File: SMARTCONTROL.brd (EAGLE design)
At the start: 40 x 50 mm, 37 parts, among them IC1 ESP12SMT, Q2 RJU003N03, Q3 RJU003N03, Q4 RJU003N03, Q5 RJU003N03

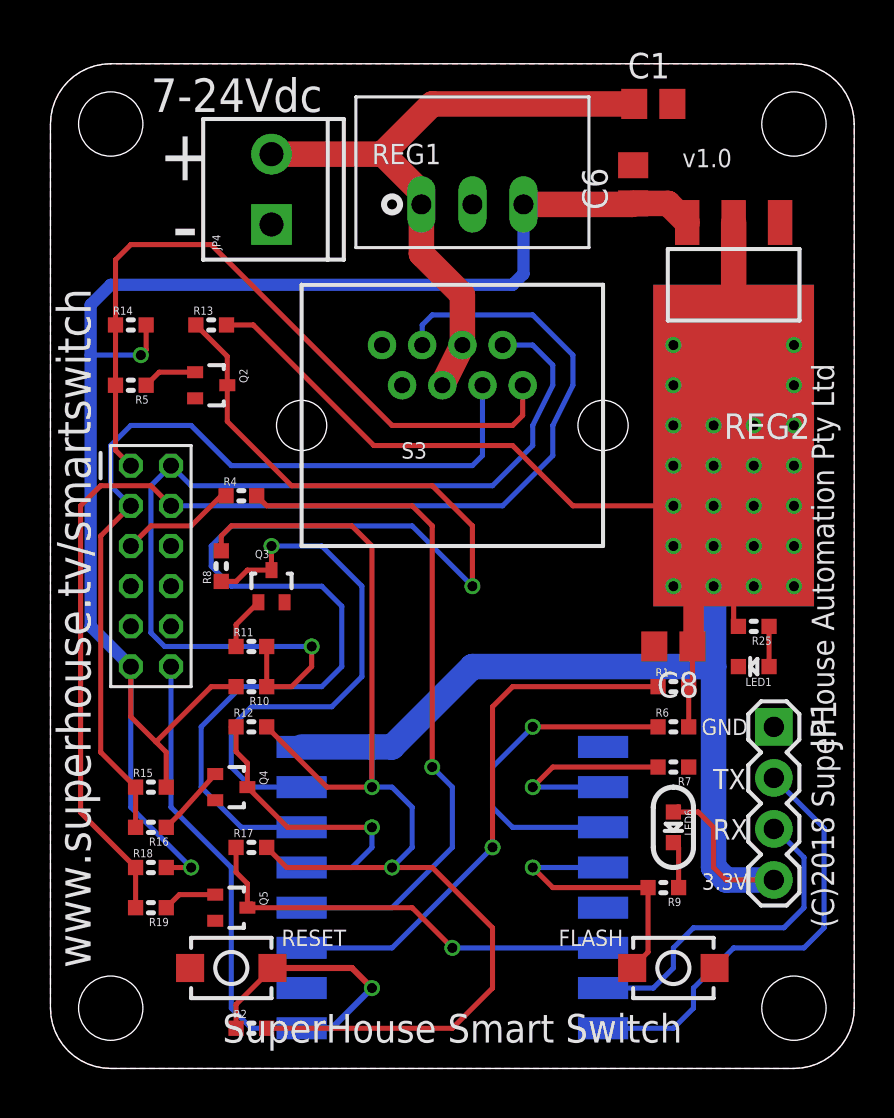
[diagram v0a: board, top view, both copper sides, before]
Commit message: Fixed ESP-12 footprint (swapped D4/5)
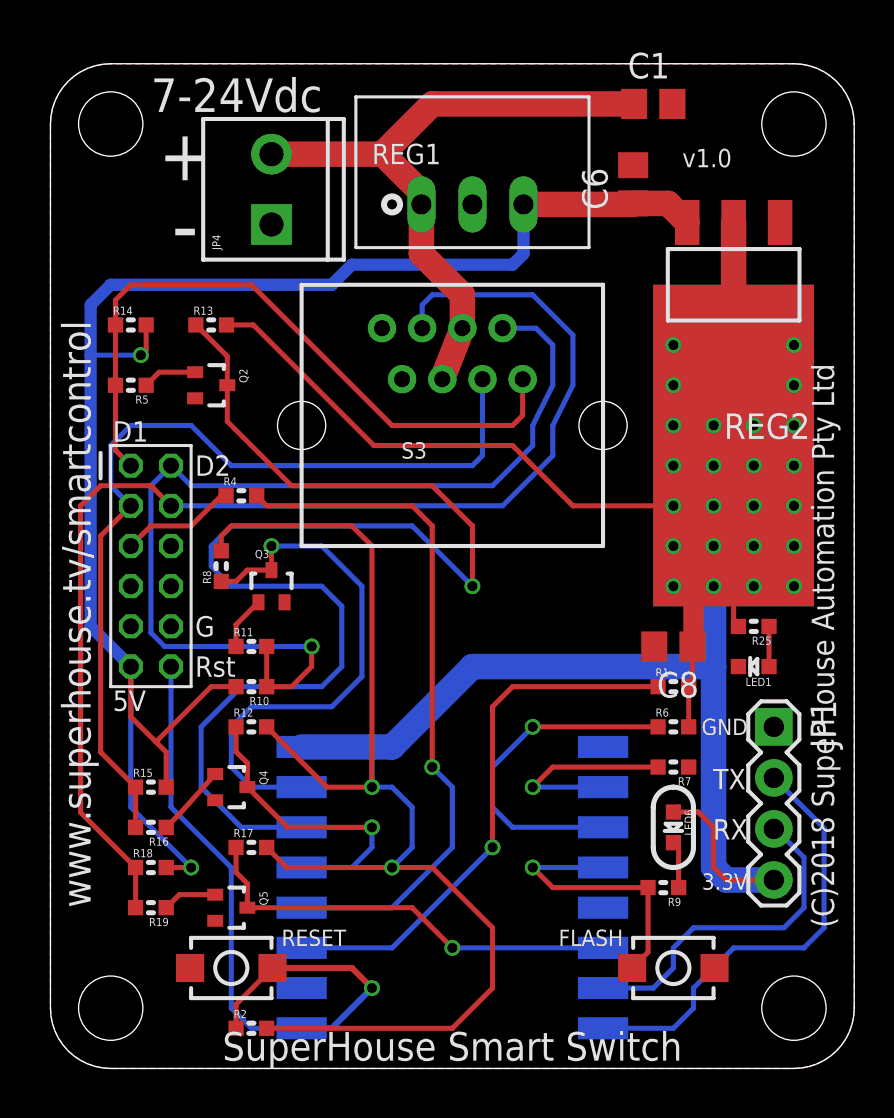
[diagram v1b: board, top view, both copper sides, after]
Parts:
- R4: value 330R -> 100R
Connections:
- net GPIO4: now also IC1.13; no longer IC1.14, Q5.3, R17.1
- net GPIO5: now also IC1.14, Q5.3, R17.1; no longer IC1.13
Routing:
- net GPIO4: track 22.0 -> 0.00 mm, vias 1 -> 0
- net GPIO5: track 0.00 -> 21.8 mm, vias 0 -> 1
- net BUTTON1: track 36.6 -> 34.0 mm
- net BUTTON4: track 61.3 -> 62.4 mm
- net BUTTON2: track 49.1 -> 50.0 mm
- net 5V: track 81.5 -> 80.9 mm
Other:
- board text added: "5V"
- board text added: "D1"
- board text added: "D2"
- board text added: "G"
- board text added: "Rst"
- board text added: "www.superhouse.tv/smartcontrol"
- board text removed: "www.superhouse.tv/smartswitch"
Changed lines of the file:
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@@
 <text x="39" y="7" size="1.1176" layer="21" font="vector" ratio="15" rot="R90">(C)2018 SuperHouse Automation Pty Ltd</text>
 <text x="31.4452" y="44.8486" size="0.9144" layer="21" font="vector" ratio="15">v1.0</text>
-<text x="20" y="2" size="1.4224" layer="21" font="vector" ratio="15" align="center">SuperHouse Smart Switch</text>
-<text x="2" y="5" size="1.6764" layer="21" font="vector" ratio="15" rot="R90">www.superhouse.tv/smartswitch</text>
+<text x="20" y="1.1" size="1.4224" layer="21" font="vector" ratio="15" align="center">SuperHouse Smart Switch</text>
+<text x="2" y="8" size="1.4224" layer="21" font="vector" ratio="15" rot="R90">www.superhouse.tv/smartcontrol</text>
 <hole x="3" y="3" drill="3.2"/>
 <hole x="3" y="47" drill="3.2"/>
@@
 <text x="11.5" y="6.5" size="0.8128" layer="21" font="vector" ratio="14" align="center-left">RESET</text>
 <text x="28.5" y="6.5" size="0.8128" layer="21" font="vector" ratio="14" align="center-right">FLASH</text>
+<text x="7.2" y="30" size="1.016" layer="21" font="vector" ratio="18" align="center-left">D2</text>
+<text x="7.2" y="22" size="1.016" layer="21" font="vector" ratio="18" align="center-left">G</text>
+<text x="7.2" y="20" size="1.016" layer="21" font="vector" ratio="18" align="center-left">Rst</text>
+<text x="3.1" y="31.7" size="1.016" layer="21" font="vector" ratio="18" align="center-left">D1</text>
+<text x="3.1" y="18.3" size="1.016" layer="21" font="vector" ratio="18" align="center-left">5V</text>
 </plain>
 <attributes>
@@
 </autorouter>
 <elements>
-<element name="R4" library="freetronics-master-v1" package="0603" value="330R" x="9.5" y="28.5"/>
+<element name="R4" library="freetronics-master-v1" package="0603" value="100R" x="9.5" y="28.5"/>
 <element name="IC1" library="freetronics-jon" package="ESP12" value="ESP12SMT" x="20" y="6" rot="MR90"/>
 <element name="R1" library="freetronics-jon" package="0603" value="10k" x="31" y="19"/>
@@
 <wire x1="5.25" y1="16.25" x2="4" y2="17.5" width="0.254" layer="1"/>
 <wire x1="4" y1="17.5" x2="4" y2="20" width="0.254" layer="1"/>
-<wire x1="3" y1="39" x2="23" y2="39" width="0.6096" layer="16"/>
-<wire x1="23" y1="39" x2="23.54" y2="39.54" width="0.6096" layer="16"/>
-<wire x1="23.54" y1="39.54" x2="23.54" y2="43" width="0.6096" layer="16"/>
+<wire x1="3" y1="39" x2="14" y2="39" width="0.6096" layer="16"/>
+<wire x1="14" y1="39" x2="15" y2="40" width="0.6096" layer="16"/>
+<wire x1="15" y1="40" x2="23" y2="40" width="0.6096" layer="16"/>
+<wire x1="23" y1="40" x2="23.54" y2="40.54" width="0.6096" layer="16"/>
+<wire x1="23.54" y1="40.54" x2="23.54" y2="43" width="0.6096" layer="16"/>
 <wire x1="5.762" y1="10" x2="7" y2="10" width="0.254" layer="1"/>
 <via x="7" y="10" extent="1-16" drill="0.5"/>
@@
 </signal>
 <signal name="GPIO5">
-<contactref element="IC1" pad="13"/>
-</signal>
-<signal name="GPIO4">
 <contactref element="IC1" pad="14"/>
 <contactref element="Q5" pad="3"/>
 <contactref element="R17" pad="1"/>
+<wire x1="9.238" y1="11" x2="9.238" y2="9.762" width="0.254" layer="1"/>
+<wire x1="9.8" y1="9.2" x2="9.8" y2="8" width="0.254" layer="1"/>
+<wire x1="9.238" y1="9.762" x2="9.8" y2="9.2" width="0.254" layer="1"/>
 <wire x1="9.8" y1="8" x2="18" y2="8" width="0.254" layer="1"/>
 <wire x1="18" y1="8" x2="20" y2="6" width="0.254" layer="1"/>
 <via x="20" y="6" extent="1-16" drill="0.5"/>
 <wire x1="20" y1="6" x2="27.5" y2="6" width="0.254" layer="16"/>
-<wire x1="9.8" y1="8" x2="10" y2="8.2" width="0.254" layer="1"/>
-<wire x1="9.238" y1="11" x2="9.238" y2="9.762" width="0.254" layer="1"/>
-<wire x1="9.8" y1="9.2" x2="9.8" y2="8" width="0.254" layer="1"/>
-<wire x1="9.238" y1="9.762" x2="9.8" y2="9.2" width="0.254" layer="1"/>
+</signal>
+<signal name="GPIO4">
+<contactref element="IC1" pad="13"/>
 </signal>
 <signal name="GPIO14">
@@
 <wire x1="6" y1="28" x2="22.5" y2="28" width="0.254" layer="16"/>
 <wire x1="22.5" y1="28" x2="25" y2="30.5" width="0.254" layer="16"/>
-<wire x1="26" y1="35.5" x2="24" y2="37.5" width="0.254" layer="16"/>
-<wire x1="24" y1="37.5" x2="19" y2="37.5" width="0.254" layer="16"/>
-<wire x1="19" y1="37.5" x2="18.5" y2="37" width="0.254" layer="16"/>
-<wire x1="18.5" y1="37" x2="18.5" y2="36" width="0.254" layer="16"/>
+<wire x1="26" y1="36.5" x2="24" y2="38.5" width="0.254" layer="16"/>
+<wire x1="24" y1="38.5" x2="19" y2="38.5" width="0.254" layer="16"/>
+<wire x1="19" y1="38.5" x2="18.5" y2="38" width="0.254" layer="16"/>
+<wire x1="18.5" y1="38" x2="18.5" y2="36.84" width="0.254" layer="16"/>
 <wire x1="25" y1="30.5" x2="25" y2="32" width="0.254" layer="16"/>
 <wire x1="25" y1="32" x2="26" y2="34" width="0.254" layer="16"/>
-<wire x1="26" y1="34" x2="26" y2="35.5" width="0.254" layer="16"/>
+<wire x1="26" y1="34" x2="26" y2="36.5" width="0.254" layer="16"/>
 </signal>
 <signal name="BUTTON1">
@@
 <contactref element="H1" pad="1"/>
 <wire x1="3.238" y1="37" x2="3.238" y2="34" width="0.254" layer="1"/>
-<wire x1="23.5" y1="34" x2="23.5" y2="32.5" width="0.254" layer="1"/>
+<wire x1="23.5" y1="34.3" x2="23.5" y2="32.5" width="0.254" layer="1"/>
 <wire x1="23.5" y1="32.5" x2="23" y2="32" width="0.254" layer="1"/>
 <wire x1="23" y1="32" x2="17" y2="32" width="0.254" layer="1"/>
-<wire x1="17" y1="32" x2="8" y2="41" width="0.254" layer="1"/>
-<wire x1="4" y1="41" x2="3.238" y2="40.238" width="0.254" layer="1"/>
-<wire x1="3.238" y1="40.238" x2="3.238" y2="37" width="0.254" layer="1"/>
-<wire x1="8" y1="41" x2="4" y2="41" width="0.254" layer="1"/>
+<wire x1="17" y1="32" x2="10" y2="39" width="0.254" layer="1"/>
+<wire x1="4" y1="39" x2="3.238" y2="38.238" width="0.254" layer="1"/>
+<wire x1="3.238" y1="38.238" x2="3.238" y2="37" width="0.254" layer="1"/>
+<wire x1="10" y1="39" x2="4" y2="39" width="0.254" layer="1"/>
 <wire x1="3.238" y1="34" x2="3.238" y2="30.762" width="0.254" layer="1"/>
 <wire x1="3.238" y1="30.762" x2="4" y2="30" width="0.254" layer="1"/>
@@
 <wire x1="24" y1="31" x2="24" y2="32" width="0.254" layer="16"/>
 <wire x1="24" y1="32" x2="25" y2="34" width="0.254" layer="16"/>
-<wire x1="25" y1="34" x2="25" y2="35" width="0.254" layer="16"/>
-<wire x1="25" y1="35" x2="24" y2="36" width="0.254" layer="16"/>
-<wire x1="24" y1="36" x2="22.5" y2="36" width="0.254" layer="16"/>
+<wire x1="25" y1="34" x2="25" y2="36" width="0.254" layer="16"/>
 <wire x1="5" y1="29" x2="6" y2="30" width="0.254" layer="16"/>
 <via x="13" y="21" extent="1-16" drill="0.5"/>
@@
 <wire x1="5.67996875" y1="21" x2="5" y2="21.67996875" width="0.254" layer="16"/>
 <wire x1="5" y1="21.67996875" x2="5" y2="29" width="0.254" layer="16"/>
+<wire x1="25" y1="36" x2="24.16" y2="36.84" width="0.254" layer="16"/>
+<wire x1="24.16" y1="36.84" x2="22.5" y2="36.84" width="0.254" layer="16"/>
 </signal>
 <signal name="BUTTON3">
@@
 <wire x1="9" y1="30" x2="21" y2="30" width="0.254" layer="16"/>
 <wire x1="21" y1="30" x2="21.5" y2="30.5" width="0.254" layer="16"/>
-<wire x1="21.5" y1="30.5" x2="21.5" y2="34" width="0.254" layer="16"/>
+<wire x1="21.5" y1="30.5" x2="21.5" y2="34.3" width="0.254" layer="16"/>
 <wire x1="7" y1="32" x2="9" y2="30" width="0.254" layer="16"/>
 <wire x1="4" y1="28" x2="3" y2="29" width="0.254" layer="16"/>
@@
 <wire x1="18.46" y1="43" x2="18.46" y2="43.59" width="1.27" layer="1"/>
 <wire x1="18.46" y1="43.59" x2="16.55" y2="45.5" width="1.27" layer="1"/>
-<wire x1="19.5" y1="34" x2="20.5" y2="36" width="1.27" layer="1"/>
+<wire x1="19.5" y1="34.3" x2="20.5" y2="36.84" width="1.27" layer="1"/>
 <wire x1="18.46" y1="40.54" x2="18.46" y2="43" width="1.27" layer="1"/>
-<wire x1="20.5" y1="36" x2="20.5" y2="38.5" width="1.27" layer="1"/>
+<wire x1="20.5" y1="36.84" x2="20.5" y2="38.5" width="1.27" layer="1"/>
 <wire x1="20.5" y1="38.5" x2="18.46" y2="40.54" width="1.27" layer="1"/>
 </signal>
@@
 </signal>
 </signals>
+<errors>
+</errors>
 </board>
 </drawing>

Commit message: Replaced most parts using SuperHouse library to add 3D models
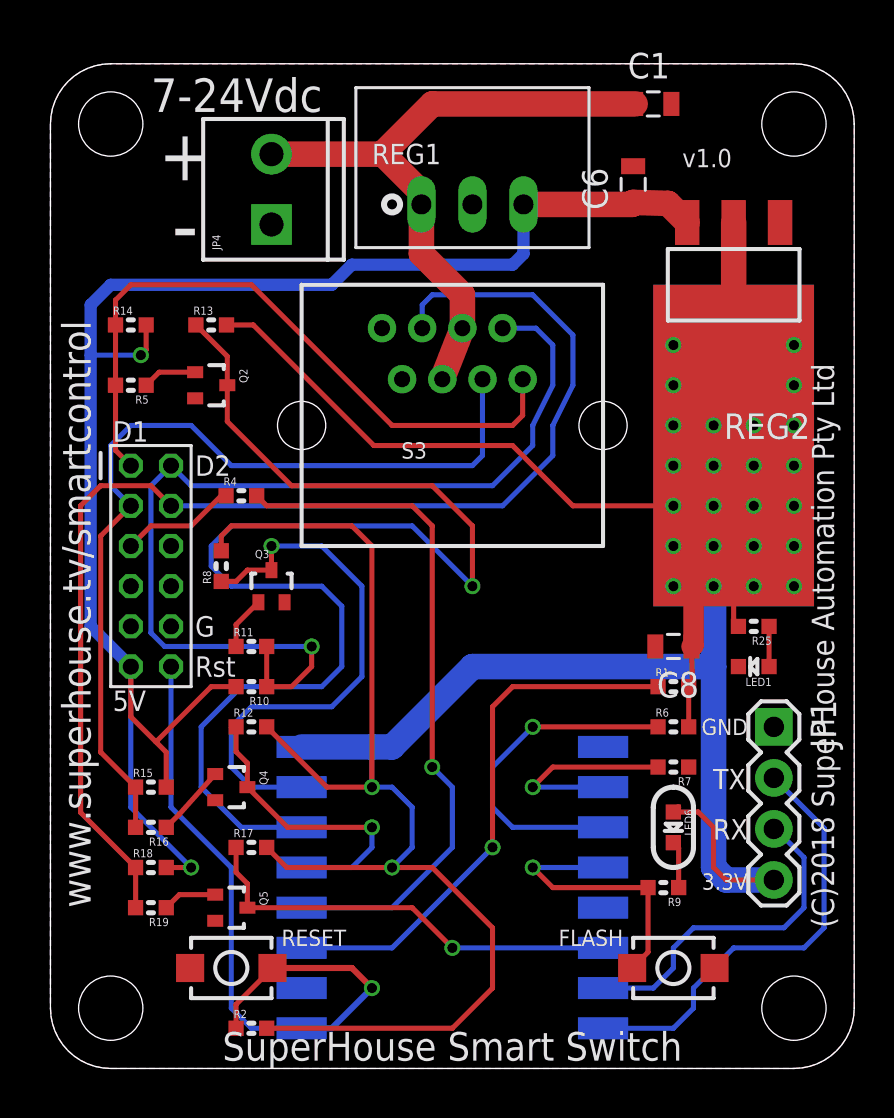
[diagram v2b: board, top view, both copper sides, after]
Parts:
- C1, C6, C8: device freetronics-jon:C0805 -> SuperHouse-DiscreteSemi:C0805
- IC1: value ESP12SMT -> ESP12-SMT; device freetronics-jon:ESP12 -> SuperHouse-MCUs:ESP12
- LED1: device freetronics-jon:LED-0603 -> SuperHouse-LEDs:LED-0603
- LED6: device freetronics-master-v1:LED-0603 -> SuperHouse-LEDs:LED-0603
- Q2, Q3, Q4, Q5: device freetronics-jon:SOT32-3 -> SuperHouse-DiscreteSemi:SOT32-3
- R1, R2, R25, R6, R7: device freetronics-jon:0603 -> SuperHouse-DiscreteSemi:R0603
- R10, R11, R12, R13, R14, R15, R16, R17, R18, R19, R4, R5, R8, R9: device freetronics-master-v1:0603 -> SuperHouse-DiscreteSemi:R0603
- REG1: device freetronics-jon:K78XX-500R3 -> SuperHouse-Regulators:K78XX-500R3
- REG2: device freetronics-luke:SOT-223 -> SuperHouse-Regulators:SOT-223
- S1, S2: device freetronics-jon:TACTILE_SWITCH_SMD_2PIN_TINY -> SuperHouse-Switches:TACTILE_SMD_3X4X2
- S3: device freetronics-jon:RJ45 -> SuperHouse-Connectors:RJ45
